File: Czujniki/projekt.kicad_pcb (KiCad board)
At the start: 2 copper layers, 136 parts, among them P1 CONN_01X02, P2 CONN_01X02, P3 CONN_01X05, P4 CONN_01X02, P5 CONN_01X04, P6 USB_OTG, SW1 SW_PUSH_SMALL, SW2 SW_PUSH_SMALL, T1 Si2323DS, T10 Si2323DS, T11 Si2323DS, T12 2N7002, T13 Si2323DS, T14 Si2323DS, T15 2N7002, T16 Si2323DS, T17 NTD25P03L, T18 2N7002, T2 2N7002, T3 2N7002, T4 NTD25P03L, T5 2N7002, T6 NTD25P03L, T7 NTD25P03L, T8 2N7002, T9 NTD25P03L, U1 MCP73831, U10 PCA9306, U11 24XX1025, U12 SHTC1, U13 HF-LPT100-10, U14 LM4041, U15 MCP6231, U2 dsPIC33EP256MU806, U3 1117, U4 1117, U5 1117, U6 MCP3201, U7 DS1338, U8 MCP6L1, U9 MCP6L1, Y1 Crystal, Y2 ZTCS

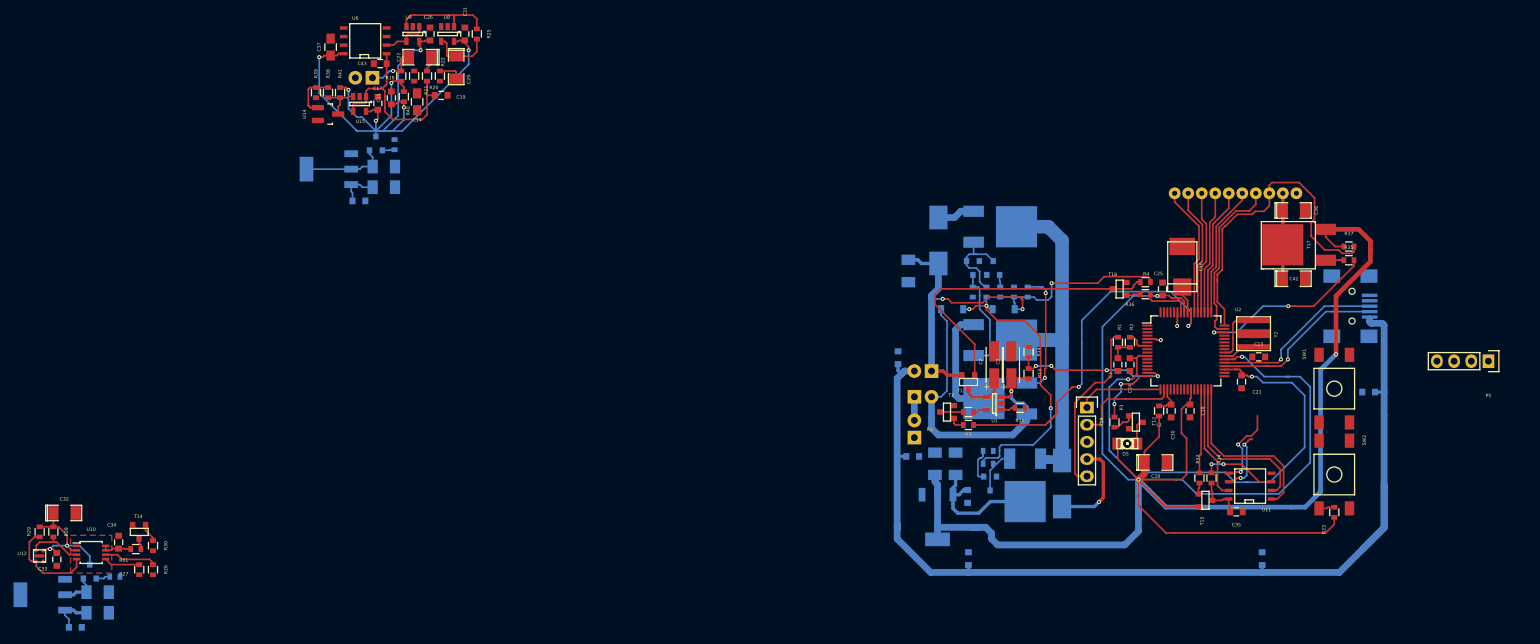
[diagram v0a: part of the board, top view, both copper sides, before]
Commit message: Working on sensor board
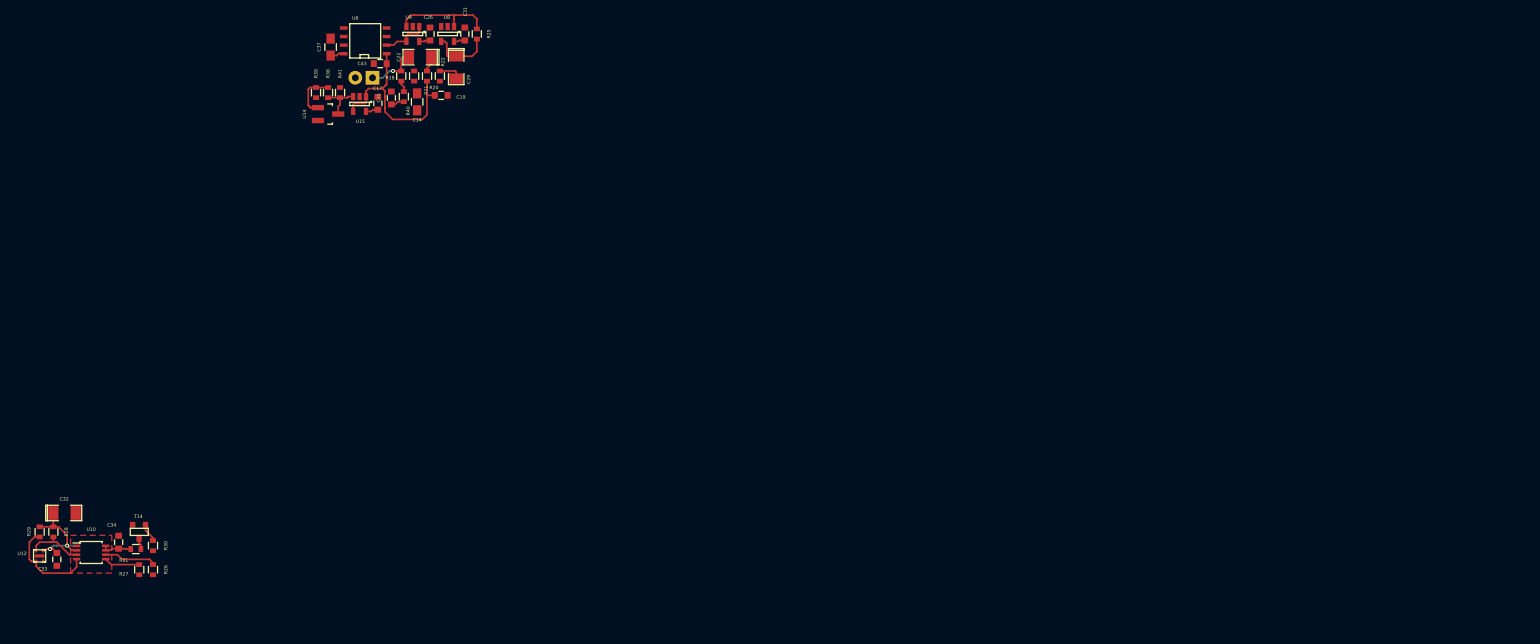
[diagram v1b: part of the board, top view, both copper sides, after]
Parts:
- removed C1, C13, C18, C20, C21, C24, C25, C30, C35, C38, C39, C4, C40, C41, C5, C9: 100N, Capacitors_SMD:C_0603_HandSoldering
- removed C10, C11, C12, C28, C36, C42, C6, C7, C8: 10U, SMD_Packages:SMD-1206_Pol
- removed C16: 10U, Capacitors_Tantalum_SMD:TantalC_SizeX_EIA-7343
- removed C2, C3: 4,7u, Footprinty:TantalC_SizeA_EIA-3216_HandSoldering
- removed C23: 100U, SMD_Packages:SMD-1206_Pol
- removed D1, D2: BAS70H, Diodes_SMD:SOD-123
- removed D3, D4: LL5817, Diodes_SMD:Diode-MELF_Handsoldering
- removed D5: LED, LEDs:LED-1206
- removed L1: 1n, Resistors_SMD:R_0603
- removed P1, P2: CONN_01X02, Pin_Headers:Pin_Header_Straight_1x02
- removed P3: CONN_01X05, Socket_Strips:Socket_Strip_Straight_1x05
- removed P4: CONN_01X02, Socket_Strips:Socket_Strip_Straight_1x02
- removed P5: CONN_01X04, Socket_Strips:Socket_Strip_Straight_1x04
- removed P6: USB_OTG, Connect:USB_Mini-B
- removed R1: 4.7K, Resistors_SMD:R_0603
- removed R10, R8: 4,7k, Resistors_SMD:R_0603
- removed R11, R12, R15, R16, R17, R19, R23, R3, R32, R34, R35, R36, R4, R5, R9: 100K, Resistors_SMD:R_0603
- removed R13, R14: 1M, Resistors_SMD:R_0603
- removed R2: 100, Resistors_SMD:R_0603
- removed R37, R7: 10K, Resistors_SMD:R_0603
- removed R6: 470K, Resistors_SMD:R_0603
- removed SW1, SW2: SW_PUSH_SMALL, Footprinty:TACT_SW_ONE_PAIR
- removed T1, T10, T11: Si2323DS, Footprinty:SOT23
- removed T12, T15, T18, T2, T3, T5, T8: 2N7002, Footprinty:2N7002-SOT23
- removed T17, T4, T6, T7, T9: NTD25P03L, SMD_Packages:DPAK-3_GDS
- removed U1: MCP73831, Housings_SOT-23_SOT-143_TSOT-6:SOT-23-5
- removed U11: 24XX1025, SMD_Packages:SOIC-8-N
- removed U13: HF-LPT100-10, Footprinty:HF-LPT100-10
- removed U2: dsPIC33EP256MU806, Housings_QFP:TQFP-64_10x10mm_Pitch0.5mm
- removed U3, U4, U5: 1117, Footprinty:SOT-223-1117
- removed Y2: ZTCS, Footprinty:ZTTCS
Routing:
- net VDD: track 390.8 -> 0.00 mm, vias 6 -> 0
- net VUSB_BUS: track 158.8 -> 0.00 mm
- net VDD2: track 93.7 -> 9.58 mm, vias 7 -> 0
- net VBUS: track 70.4 -> 0.00 mm, vias 3 -> 0
- net VINPUT: track 62.8 -> 0.00 mm
- net CHARGE_ENABLE: track 54.0 -> 0.00 mm, vias 2 -> 0
- net RL: track 48.8 -> 0.00 mm
- net VBATTERY: track 48.1 -> 0.00 mm, vias 1 -> 0
- net CHARGE_SIGNAL: track 45.7 -> 0.00 mm
- net VON: track 43.7 -> 0.00 mm, vias 3 -> 0
- net Net-(C4-Pad1): track 31.2 -> 0.00 mm
- net COMM_ENABLE: track 27.1 -> 0.00 mm, vias 2 -> 0
- net DM: track 26.4 -> 0.00 mm, vias 1 -> 0
- net MA0: track 26.2 -> 0.00 mm
- net RESET: track 25.9 -> 0.00 mm
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
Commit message: Simplifiying all
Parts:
- removed C32: 10U, SMD_Packages:SMD-1206_Pol
- added C1: 1U, Capacitors_SMD:C_0805_HandSoldering, F.Cu at (166.8, 66.3)
- added C2: 1U, Capacitors_SMD:C_0805_HandSoldering, F.Cu at (166.8, 71.2)
- added P1: CONN_01X12, Footprinty:DS1065-02-1-12S8BS, B.Cu at (180.3, 78.1)
- added REF**: 1pin, Connect:1pin, F.Cu at (210.8, 93.3)
- added REF**: 1pin, Connect:1pin, F.Cu at (160.0, 93.3)
- added REF**: 1pin, Connect:1pin, F.Cu at (160.0, 62.9)
- added REF**: 1pin, Connect:1pin, F.Cu at (210.8, 78.1)
- added U1: MCP1700, Footprinty:SOT23-mcp1700, F.Cu at (164.1, 70.6)
- moved U12 142.8 mm to (173.7, 74.5), turned to 90 degrees
- moved C33 142.3 mm to (174.3, 72.0), turned to 0 degrees
- moved R27 139.6 mm to (175.8, 59.8), turned to 0 degrees
- moved R26 139.0 mm to (175.8, 57.8), turned to 0 degrees
- moved U10 138.7 mm to (173.2, 66.9), turned to 90 degrees
- moved R29 138.1 mm to (170.2, 74.5), turned to 0 degrees
- moved R28 137.1 mm to (170.2, 72.5), turned to 0 degrees
- moved R31 135.6 mm to (172.7, 60.3), turned to 270 degrees
- moved C34 135.0 mm to (171.7, 62.8), turned to 180 degrees
- moved R30 134.1 mm to (172.2, 57.8), turned to 0 degrees
- moved T14 131.9 mm to (170.2, 59.8), turned to 270 degrees
- moved CE1 110.5 mm to (166.3, 97.5), turned to 90 degrees
- moved T16 106.8 mm to (169.6, 94.4), turned to 90 degrees
- moved R33 106.0 mm to (169.6, 97.1), turned to 180 degrees
- moved C31 102.6 mm to (205.4, 82.5)
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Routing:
- net PRESS_ENABLE: track 0.00 -> 37.8 mm, vias 0 -> 1
- net CLOCK_ENABLE: track 0.00 -> 30.9 mm, vias 0 -> 1
- net SDA: track 5.30 -> 32.7 mm, vias 0 -> 1
- net SCL: track 7.76 -> 34.4 mm, vias 0 -> 1
- net MAIN_VOL: track 0.00 -> 20.1 mm, vias 0 -> 1
- net Net-(BT1-Pad1): track 0.00 -> 15.5 mm
- net SUSPEND: track 0.00 -> 15.2 mm, vias 0 -> 1
- net ADCDATA: track 0.00 -> 15.1 mm, vias 0 -> 1
- net CLOCK: track 0.00 -> 14.9 mm, vias 0 -> 1
- net +1V8: track 16.8 -> 20.1 mm
- net VDD2: track 9.58 -> 7.55 mm
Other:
- board outline added: 55.9 x 45.7 mm

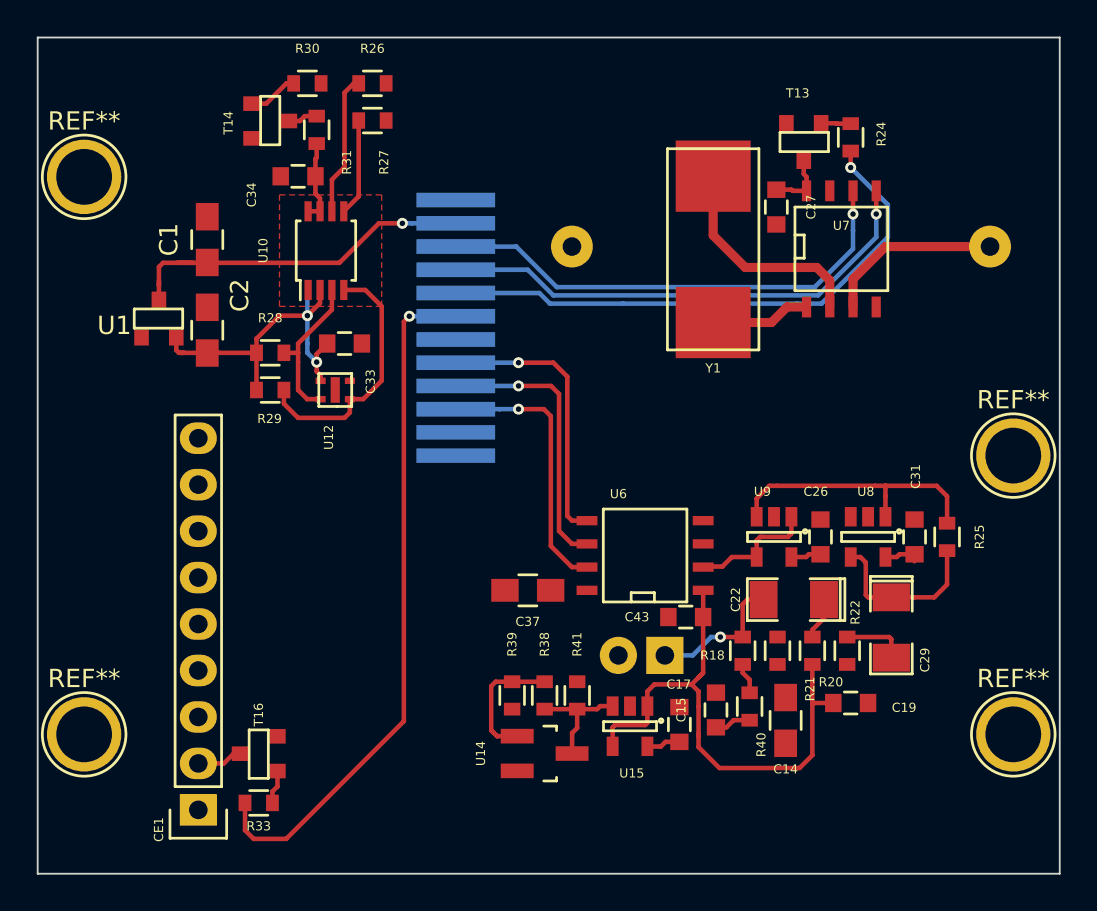
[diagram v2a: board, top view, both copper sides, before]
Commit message: DC/DC converter to linear converter change
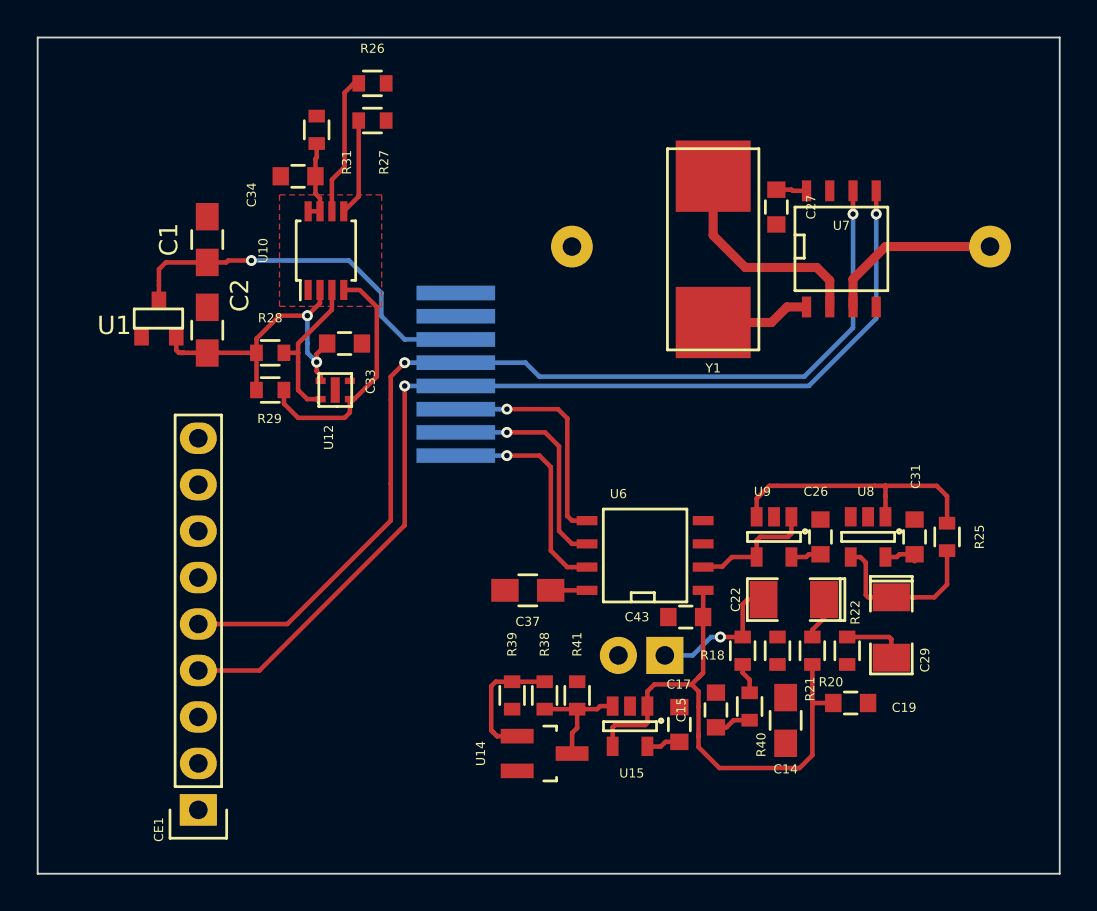
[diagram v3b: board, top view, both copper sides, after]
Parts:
- removed R24, R33: 100K, Resistors_SMD:R_0603
- removed R30: 220K, Resistors_SMD:R_0603
- removed REF** (x4): 1pin, Connect:1pin
- removed T13, T14, T16: Si2323DS, Footprinty:SOT23
- P1: value CONN_01X12 -> CONN_01X08; footprint Footprinty:DS1065-02-1-12S8BS -> Footprinty:DS1065-02-1X8S8BS
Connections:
- C15 pad 1: VDD2 -> VDD
- C17 pad 1: VDD2 -> VDD
- C26 pad 1: VDD2 -> VDD
- C27 pad 1: Net-(C27-Pad1) -> VDD
- C31 pad 1: VDD2 -> VDD
- C37 pad 1: VDD2 -> VDD
- CE1 pad 2: Net-(CE1-Pad2) -> VDD
- P1 pad 1: (no net) -> CLOCK
- P1 pad 2: CONV_ENABLE -> ADCDATA
- P1 pad 3: CLOCK -> SUSPEND
- P1 pad 4: ADCDATA -> SDA
- P1 pad 5: SUSPEND -> SCL
- P1 pad 6: (no net) -> MAIN_VOL
- P1 pad 7: PRESS_ENABLE -> (no net)
- P1 pad 8: CLOCK_ENABLE -> GND
- R31 pad 1: Net-(R31-Pad1) -> VDD
- R40 pad 1: VDD2 -> VDD
- R41 pad 1: VDD2 -> VDD
- U15 pad 5: VDD2 -> VDD
- U6 pad 8: VDD2 -> VDD
- U7 pad 8: Net-(C27-Pad1) -> VDD
- U8 pad 5: VDD2 -> VDD
- U9 pad 5: VDD2 -> VDD
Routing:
- net PRESS_ENABLE: track 37.8 -> 0.00 mm, vias 1 -> 0
- net CLOCK_ENABLE: track 30.9 -> 0.00 mm, vias 1 -> 0
- net SDA: track 32.7 -> 61.8 mm, vias 1 -> 2
- net SCL: track 34.4 -> 63.0 mm, vias 1 -> 2
- net VDD: track 0.00 -> 11.2 mm
- net VDD2: track 7.55 -> 0.00 mm
- net Net-(C27-Pad1): track 3.38 -> 0.00 mm
- net Net-(R30-Pad1): track 2.77 -> 0.00 mm
- net ADCDATA: track 15.1 -> 12.4 mm
- net CLOCK: track 14.9 -> 12.4 mm
- net Net-(CE1-Pad2): track 2.50 -> 0.00 mm
- net SUSPEND: track 15.2 -> 12.8 mm
- net Net-(R33-Pad1): track 1.86 -> 0.00 mm
- net +1V8: track 20.1 -> 18.3 mm
- net Net-(R31-Pad1): track 1.63 -> 0.00 mm
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
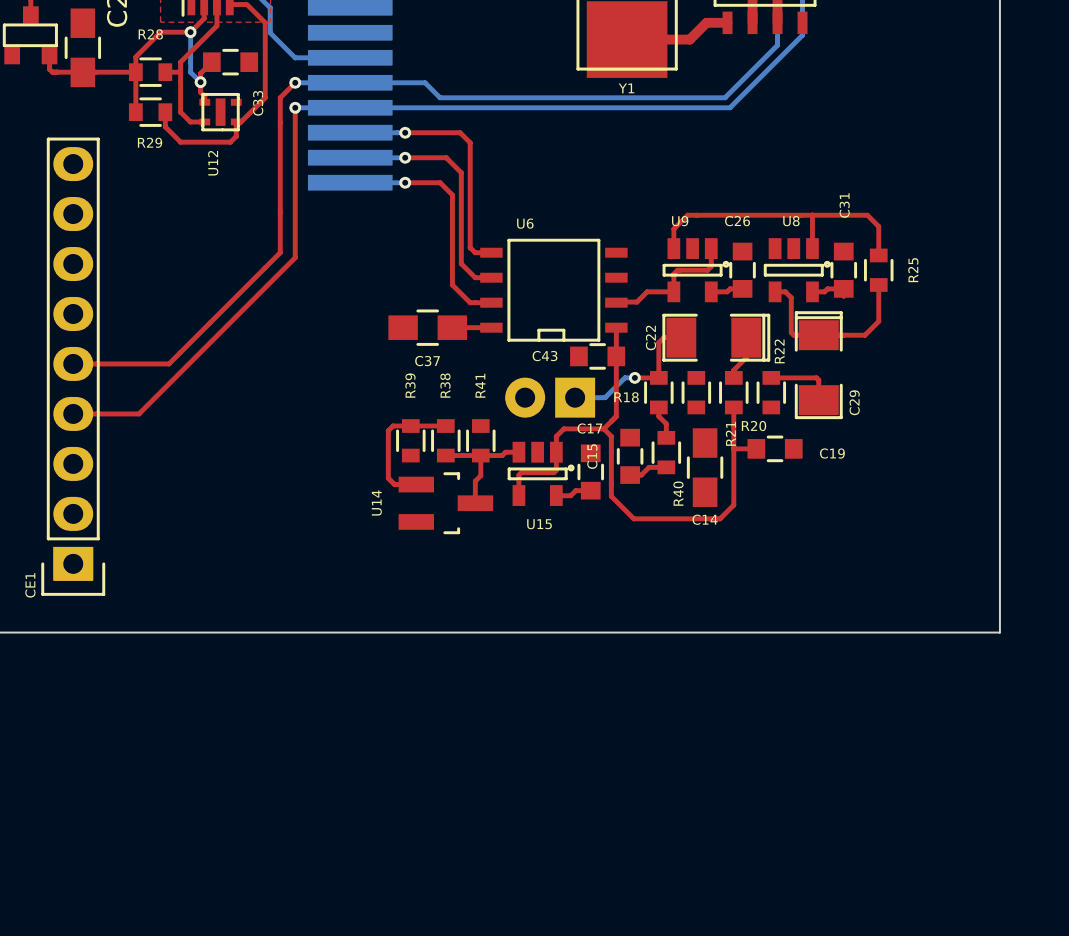
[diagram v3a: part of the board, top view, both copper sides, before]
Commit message: Edits + additional program for dust controller
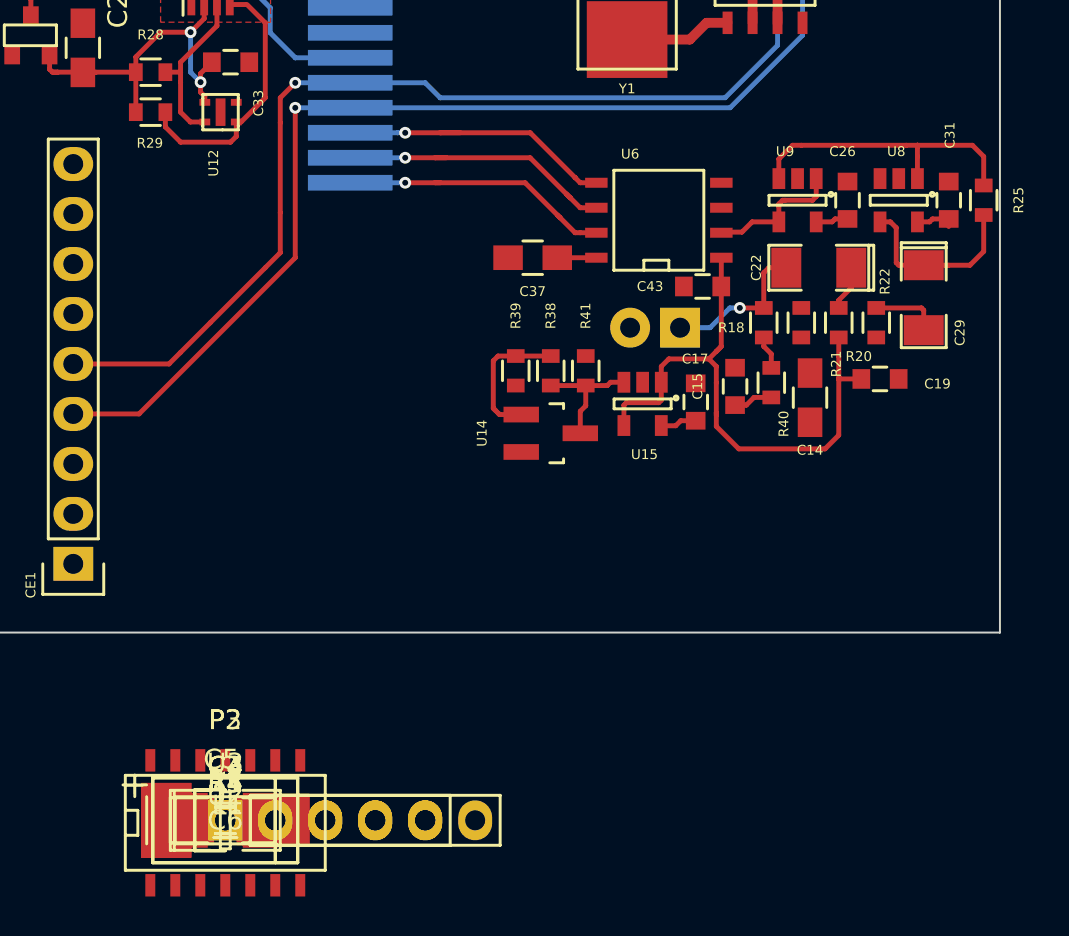
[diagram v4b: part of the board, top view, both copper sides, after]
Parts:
- added C3: 220U, Capacitors_Tantalum_SMD:TantalC_SizeX_EIA-7343, F.Cu at (174.0, 110.5)
- added C4: 10U, Capacitors_Tantalum_SMD:TantalC_SizeX_EIA-7343, F.Cu at (174.0, 110.5)
- added C5: 4,7U, Capacitors_Tantalum_SMD:TantalC_SizeA_EIA-3216_HandSoldering, F.Cu at (174.0, 110.5)
- added C6: 10U, SMD_Packages:SMD-1206_Pol, F.Cu at (174.0, 110.5)
- added L1: NLCV32T-4R7M-PF, SMD_Packages:SMD-1210_Pol, F.Cu at (174.0, 110.5)
- added P2: CONN_01X06, Socket_Strips:Socket_Strip_Straight_1x06, F.Cu at (174.0, 110.5)
- added P3: CONN_01X05, Socket_Strips:Socket_Strip_Straight_1x05, F.Cu at (174.0, 110.5)
- added R1: 100, Resistors_SMD:R_0603, F.Cu at (174.0, 110.5)
- added R2: 150, Resistors_SMD:R_0805, F.Cu at (174.0, 110.5)
- added R3: 3M, Resistors_SMD:R_0603, F.Cu at (174.0, 110.5)
- added R4: 1M, Resistors_SMD:R_0603, F.Cu at (174.0, 110.5)
- added R5: 4,7K, Resistors_SMD:R_0603, F.Cu at (174.0, 110.5)
- added U2: PIC16F1703, SMD_Packages:SOIC-14_N, F.Cu at (174.0, 110.5)
- added U3: MCP16251, Housings_SOT-23_SOT-143_TSOT-6:SOT-23-6, F.Cu at (174.0, 110.5)
- moved C14 6.41 mm to (203.7, 89.0)
- moved C15 6.41 mm to (199.9, 88.5)
- moved C17 6.41 mm to (197.9, 89.2)
- moved C19 6.41 mm to (207.3, 88.1)
- moved C22 6.41 mm to (204.2, 82.4)
- moved C26 6.41 mm to (205.6, 79.0)
- moved C29 6.41 mm to (209.5, 83.9)
- moved C37 6.41 mm to (189.6, 81.9)
- moved C43 6.41 mm to (198.2, 83.4)
- moved E1 6.41 mm to (197.1, 85.5)
- moved R18 6.41 mm to (201.4, 85.2)
- moved R20 6.41 mm to (205.2, 85.2)
- moved R21 6.41 mm to (203.3, 85.2)
- moved R22 6.41 mm to (207.1, 85.2)
- moved R25 6.41 mm to (212.5, 79.0)
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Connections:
- CE1 pad 2: VDD -> VDD2
- P1 pad 7: (no net) -> VDD2
- R26 pad 2: VDD -> VDD2
- R27 pad 2: VDD -> VDD2
- R31 pad 1: VDD -> VDD2
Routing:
- net ADCDATA: track 12.4 -> 14.4 mm
- net SUSPEND: track 12.8 -> 14.6 mm
- net CLOCK: track 12.4 -> 14.0 mm
